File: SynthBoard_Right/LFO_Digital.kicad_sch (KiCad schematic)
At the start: 13 parts, among them IC3 PIC16F15325-I/SL, J2 ICSP LFO, U7 MCP6234T-E/SL

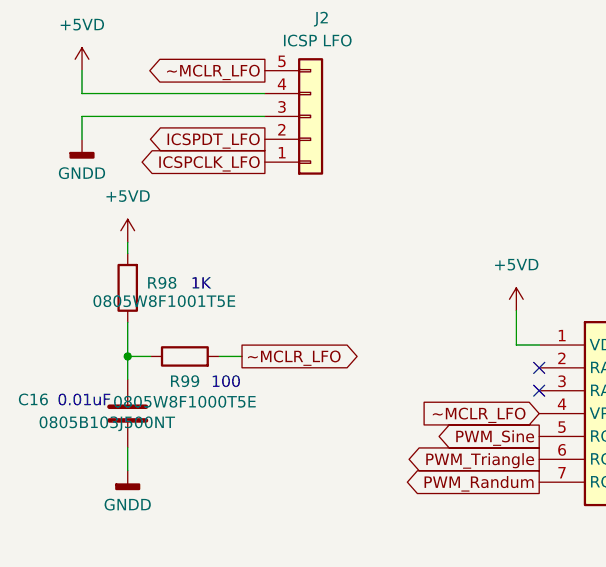
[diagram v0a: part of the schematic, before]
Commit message: SynthBoard
Rightを配置済
Leftの配線ミスを修正
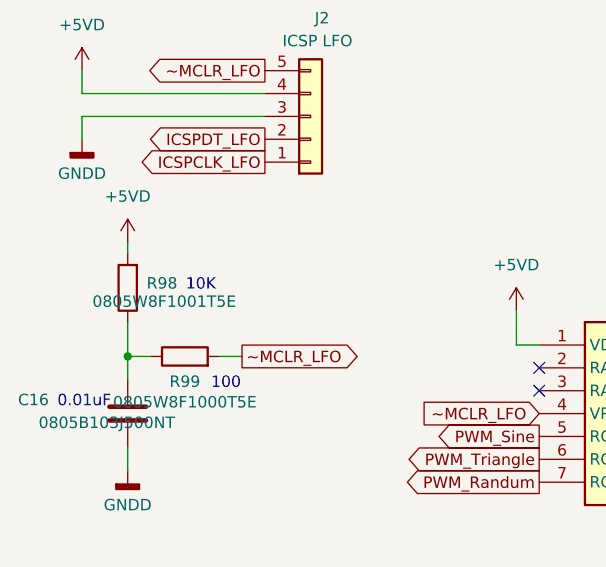
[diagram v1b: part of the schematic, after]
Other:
- note removed: "1K"
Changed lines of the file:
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@@
 	(generator_version "9.0")
 	(paper "A4")
-	(text "1K"
+	(text "10K"
 		(exclude_from_sim no)
 		(at 69.088 78.486 0)
